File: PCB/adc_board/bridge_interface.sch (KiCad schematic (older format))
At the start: 8 parts, among them J2 54-00177, U4 MAX4209HAUA

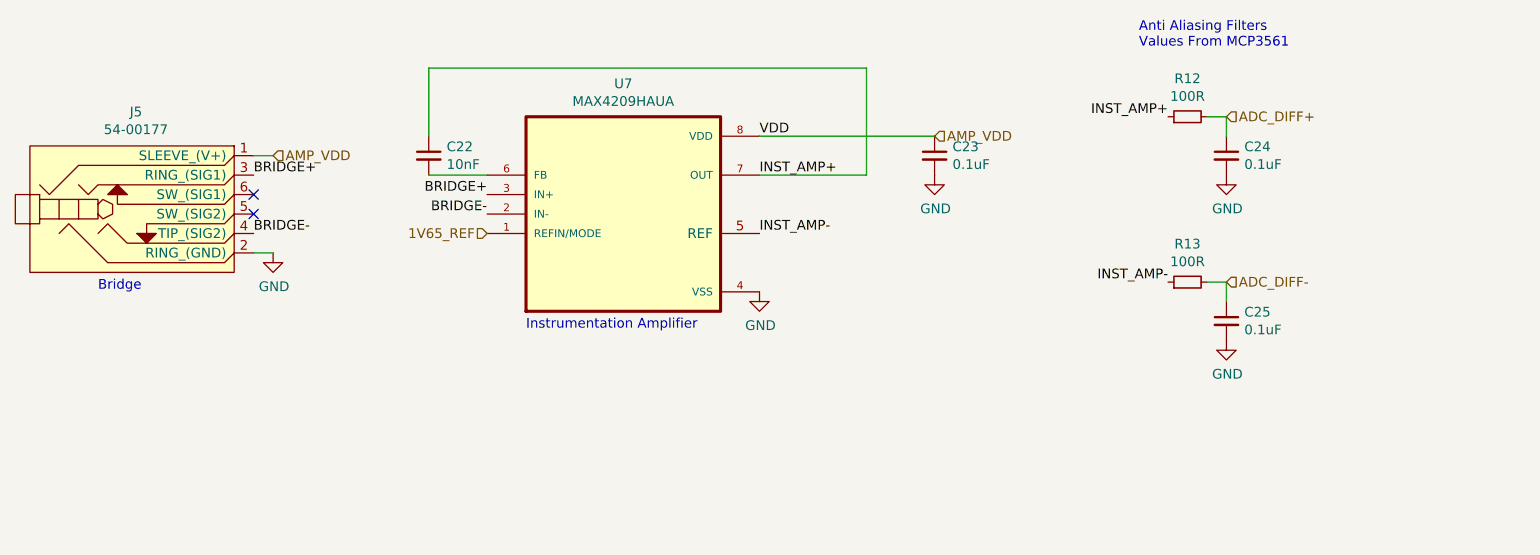
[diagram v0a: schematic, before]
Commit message: Finished layout for adc board
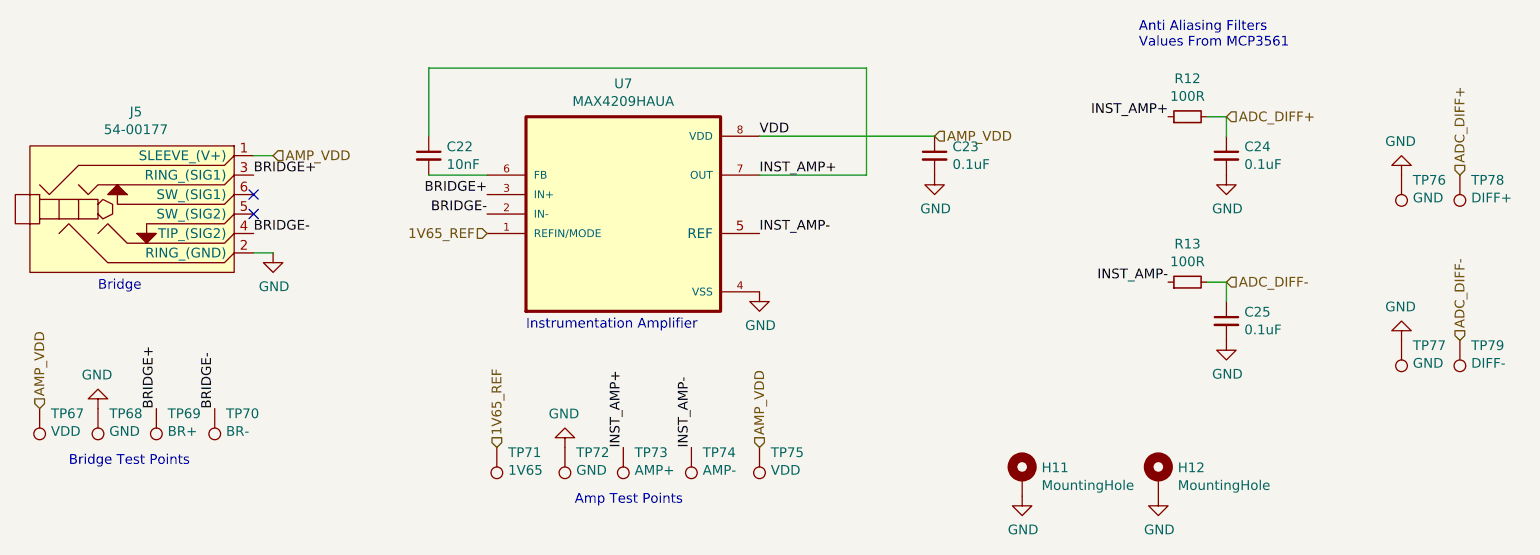
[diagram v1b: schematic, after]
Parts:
- added H11, H12: MountingHole, MountingHole:MountingHole_3.2mm_M3_Pad_Via, symbol Mechanical:MountingHole_Pad
- added TP67, TP75: VDD, TestPoint:TestPoint_Pad_D1.0mm, symbol Connector:TestPoint
- added TP68, TP72, TP76, TP77: GND, TestPoint:TestPoint_Pad_D1.0mm, symbol Connector:TestPoint
- added TP69: BR+, TestPoint:TestPoint_Pad_D1.0mm, symbol Connector:TestPoint
- added TP70: BR-, TestPoint:TestPoint_Pad_D1.0mm, symbol Connector:TestPoint
- added TP71: 1V65, TestPoint:TestPoint_Pad_D1.0mm, symbol Connector:TestPoint
- added TP73: AMP+, TestPoint:TestPoint_Pad_D1.0mm, symbol Connector:TestPoint
- added TP74: AMP-, TestPoint:TestPoint_Pad_D1.0mm, symbol Connector:TestPoint
- added TP78: DIFF+, TestPoint:TestPoint_Pad_D1.0mm, symbol Connector:TestPoint
- added TP79: DIFF-, TestPoint:TestPoint_Pad_D1.0mm, symbol Connector:TestPoint
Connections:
- net 1V65_REF: now also TP71.1
- net ADC_DIFF+: now also TP78.1
- net ADC_DIFF-: now also TP79.1
- net AMP_VDD: now also TP67.1, TP75.1
- net BRIDGE+: now also TP69.1
- net BRIDGE-: now also TP70.1
- net GND: now also H11.1, H12.1, TP68.1, TP72.1, TP76.1, TP77.1
- net INST_AMP+: now also TP73.1
- net INST_AMP-: now also TP74.1
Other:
- note added: "Amp Test Points"
- note added: "Bridge Test Points"
